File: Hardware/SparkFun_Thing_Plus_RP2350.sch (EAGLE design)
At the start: 84 parts, among them J1 THING_PLUS_LOGICAL, J3 QWIIC_RIGHT_ANGLE, J6 MICRO-SD-ATOM, Q1 100mA/20V/3.8Ω, U1 RP2350A, U2 RM2, U3 RT9080-33GJ5, U4 LM66200, U5 W25QXX128MBIT, U6 MCP73831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

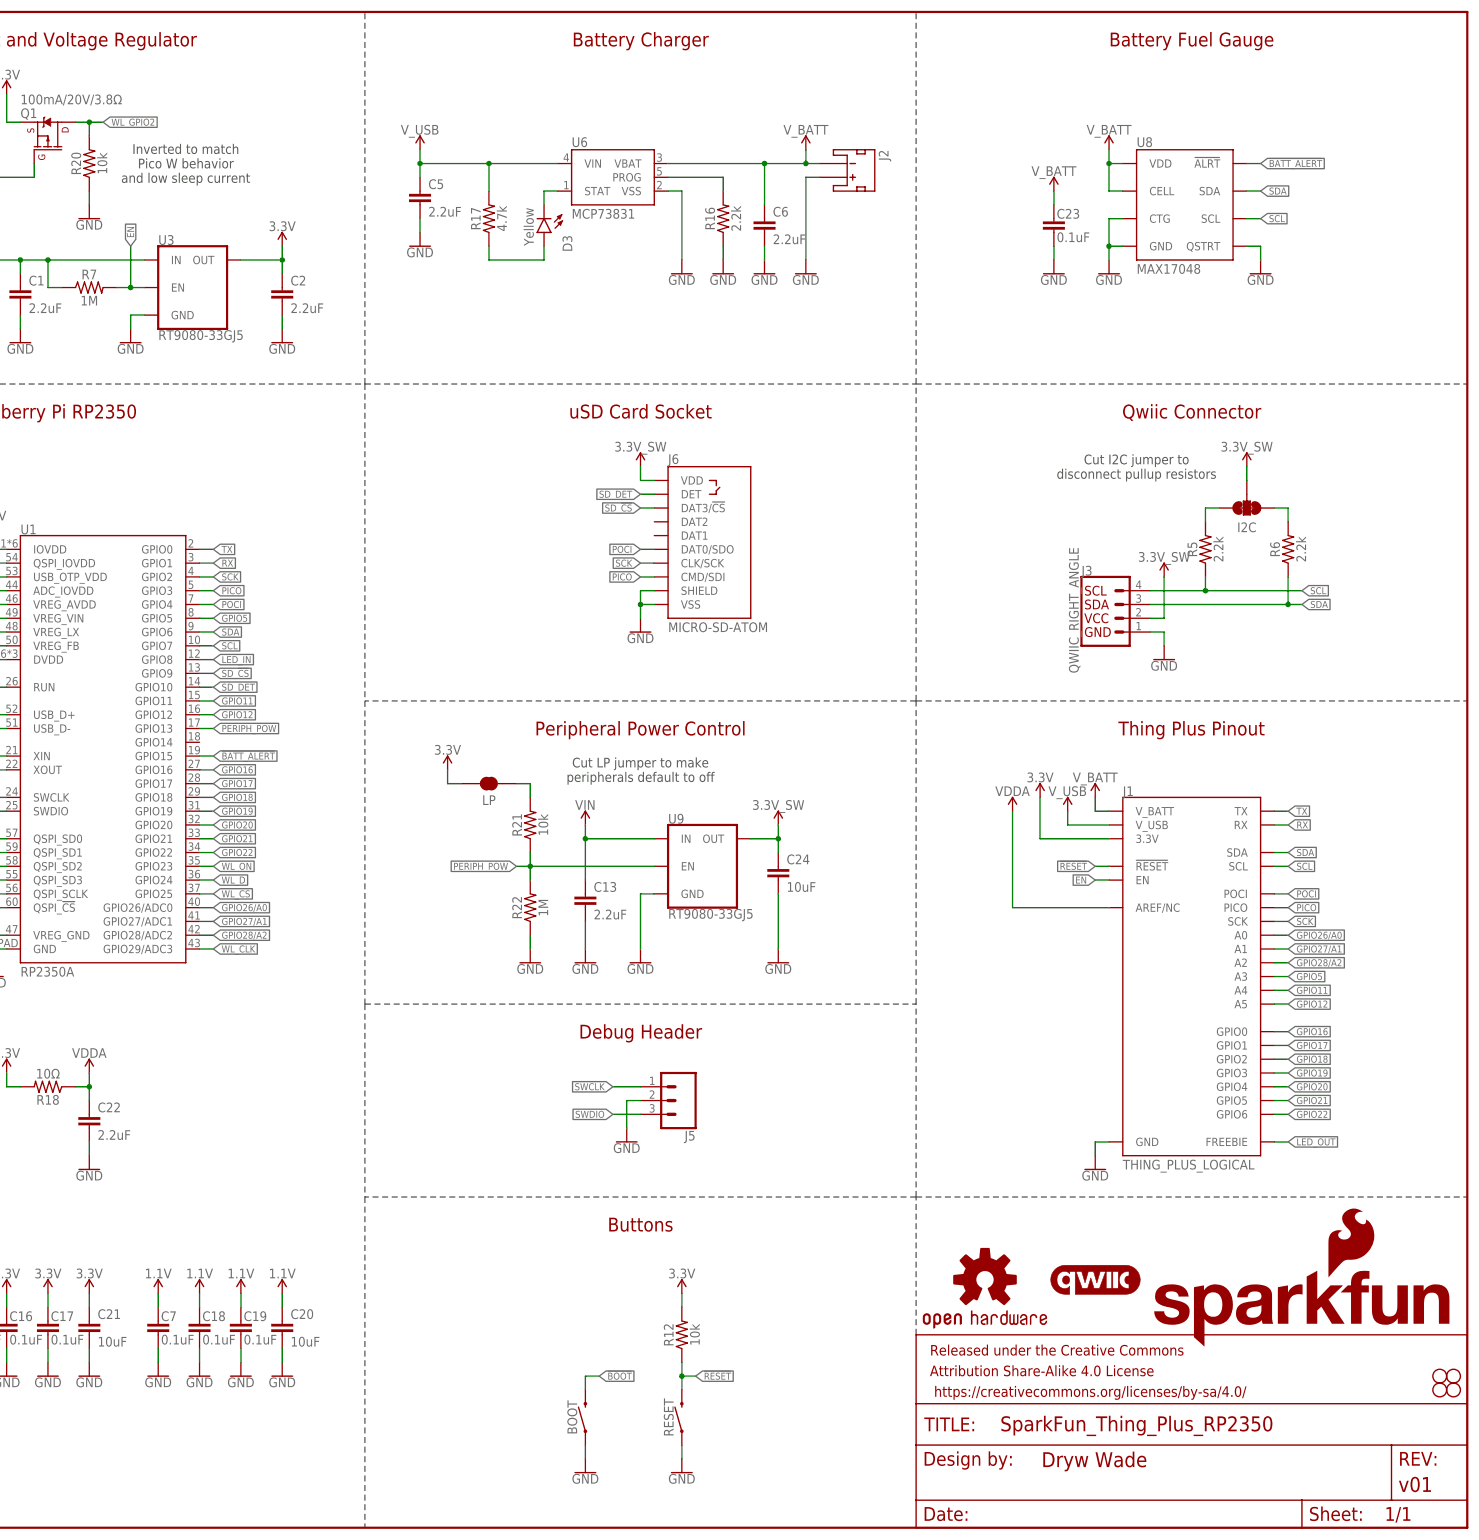
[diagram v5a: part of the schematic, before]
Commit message: Design review updates
Change version number to v02 (significant changes made since v01)
Add version number to copper
Add voltage regulator voltage and current specifications to schematic
Fix swapped POCI and PICO silk
Add test point for BOOT button
Fix acid traps
Add GND vias for each decoupling cap of U1
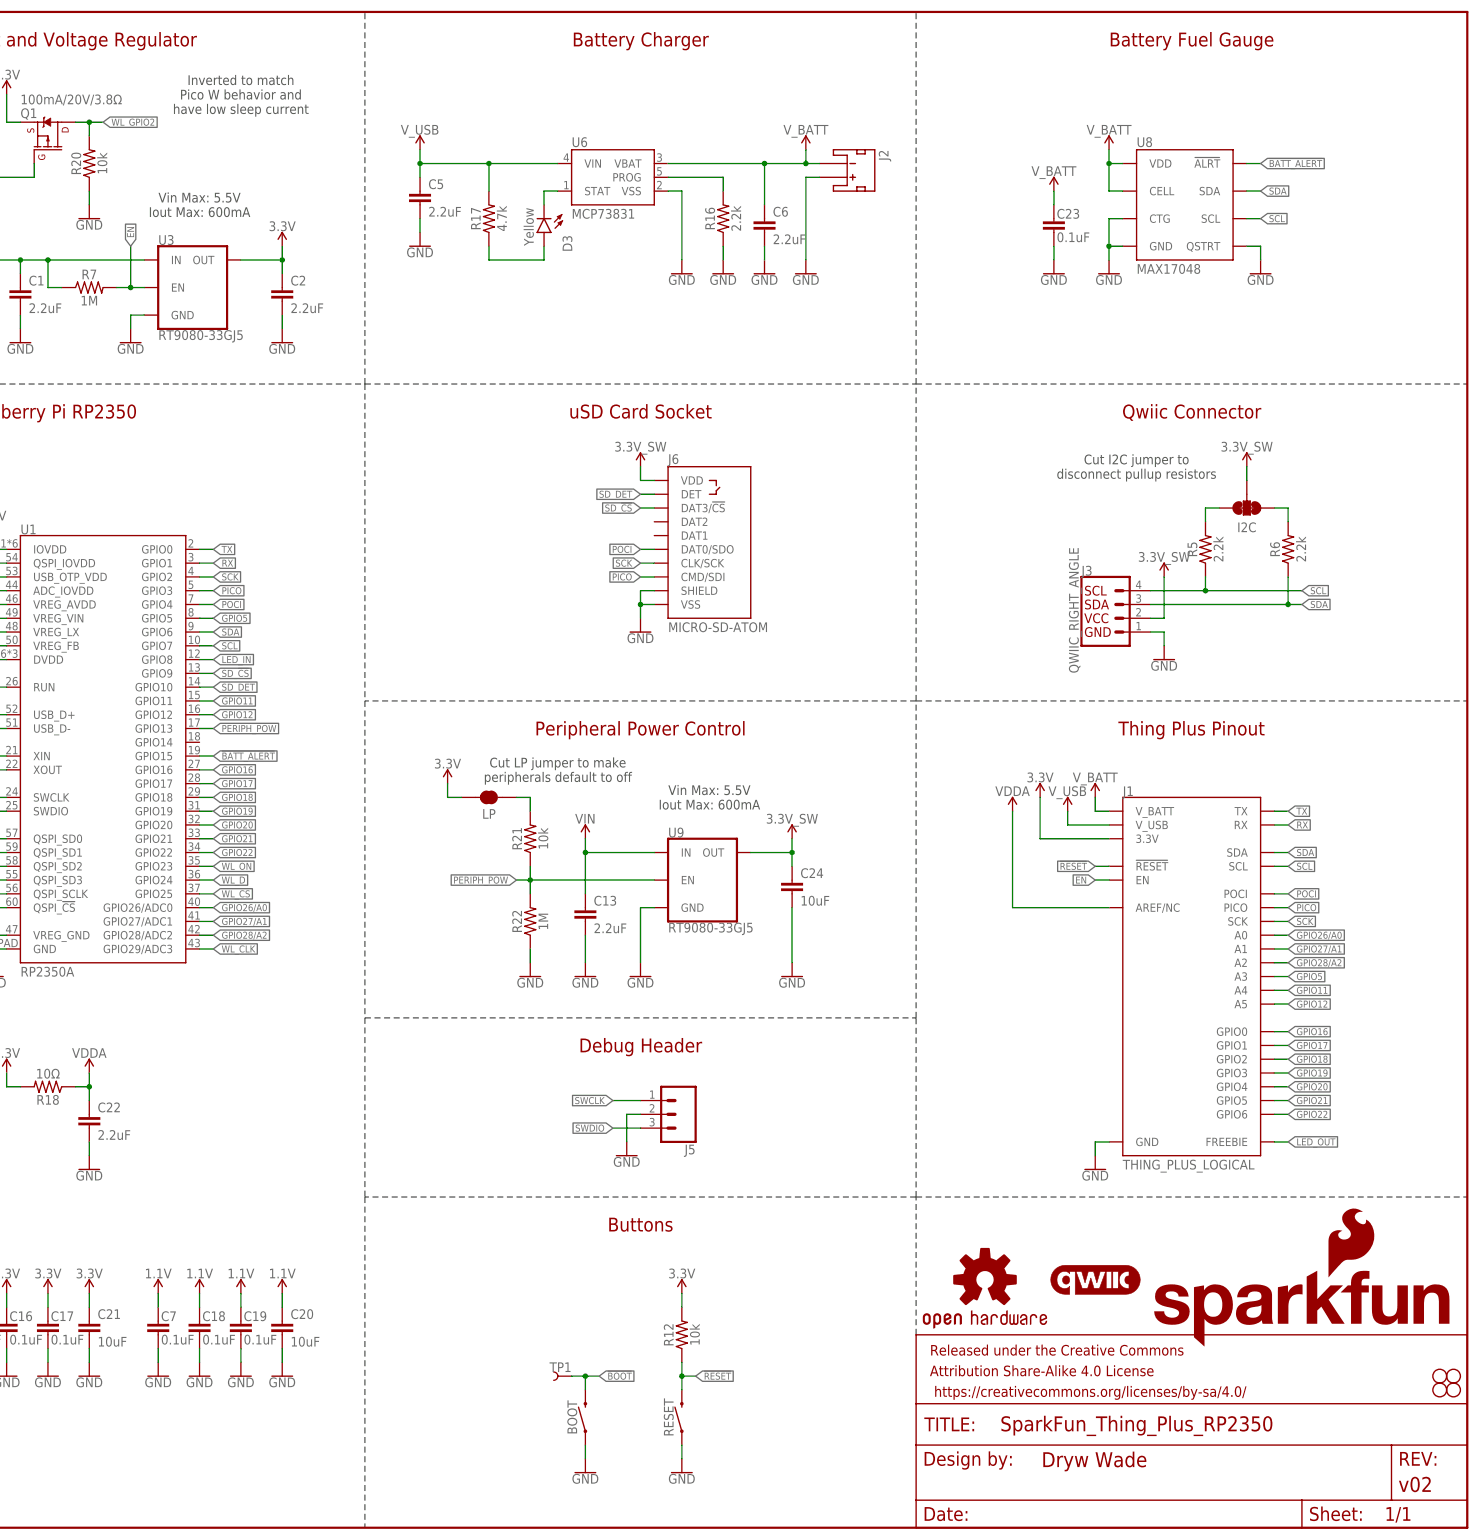
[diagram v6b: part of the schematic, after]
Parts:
- added TP1: TEST-POINT3X5, SparkFun-Connectors:TEST-POINT3X5
- FRAME1: REV v01 -> v02
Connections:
- net !BOOT!: now also TP1.1
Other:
- note added: "Inverted to match Pico W behavior and have low sleep current"
- note added: "Vin Max: 5.5V Iout Max: 600mA"
- note removed: "Inverted to match Pico W behavior and low sleep current"
- moved on the sheet: C13, C24, J5, LP, R21, R22, U9

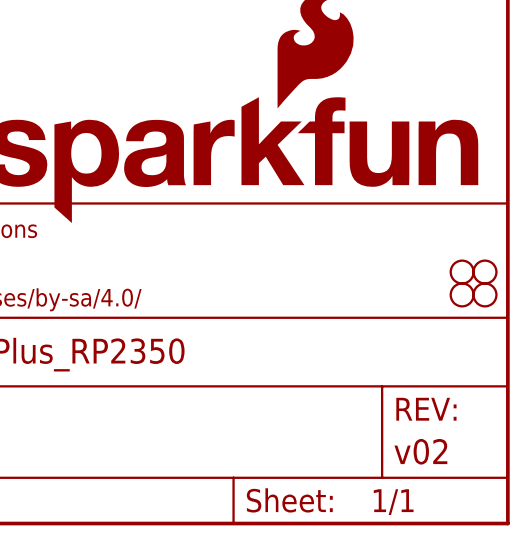
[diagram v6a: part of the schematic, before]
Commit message: Design review updates
Reposition fuel gauge and charge LED to get more clearance around them
Reposition power LED and resistor for better clearance
Add fiducials
Add measures
Fix TX and RX Buzzard tails
Fix acid trap
Improve GND pours
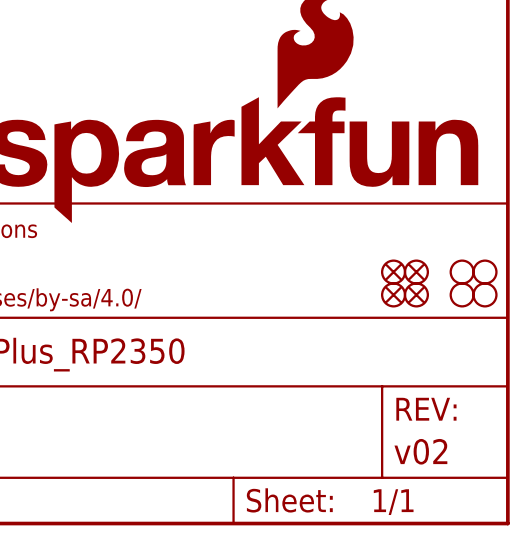
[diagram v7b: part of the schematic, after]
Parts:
- added FD1, FD2, FD3, FD4: FIDUCIALUFIDUCIAL, SparkFun-Aesthetics:FIDUCIALUFIDUCIAL
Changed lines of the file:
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@@
 <part name="SUPPLY47" library="SparkFun-PowerSymbols" deviceset="3.3V_SW" device=""/>
 <part name="TP1" library="SparkFun-Connectors" deviceset="TEST-POINT" device="3X5" value="TEST-POINT3X5"/>
+<part name="FD1" library="SparkFun-Aesthetics" deviceset="FIDUCIAL" device="UFIDUCIAL" value="FIDUCIALUFIDUCIAL"/>
+<part name="FD2" library="SparkFun-Aesthetics" deviceset="FIDUCIAL" device="UFIDUCIAL" value="FIDUCIALUFIDUCIAL"/>
+<part name="FD3" library="SparkFun-Aesthetics" deviceset="FIDUCIAL" device="UFIDUCIAL" value="FIDUCIALUFIDUCIAL"/>
+<part name="FD4" library="SparkFun-Aesthetics" deviceset="FIDUCIAL" device="UFIDUCIAL" value="FIDUCIALUFIDUCIAL"/>
 </parts>
 <sheets>
@@
 <attribute name="NAME" x="266.7" y="30.48" size="1.778" layer="95" font="vector" rot="R180"/>
 </instance>
+<instance part="FD1" gate="G$1" x="421.64" y="25.4" smashed="yes" rot="R90"/>
+<instance part="FD2" gate="G$1" x="421.64" y="27.94" smashed="yes" rot="R90"/>
+<instance part="FD3" gate="G$1" x="419.1" y="27.94" smashed="yes" rot="R90"/>
+<instance part="FD4" gate="G$1" x="419.1" y="25.4" smashed="yes" rot="R90"/>
 </instances>
 <busses>

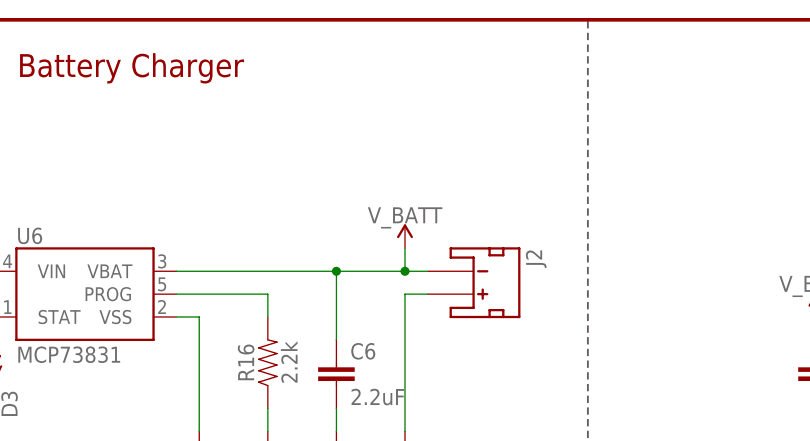
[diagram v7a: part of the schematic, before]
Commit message: Improve GND stitching
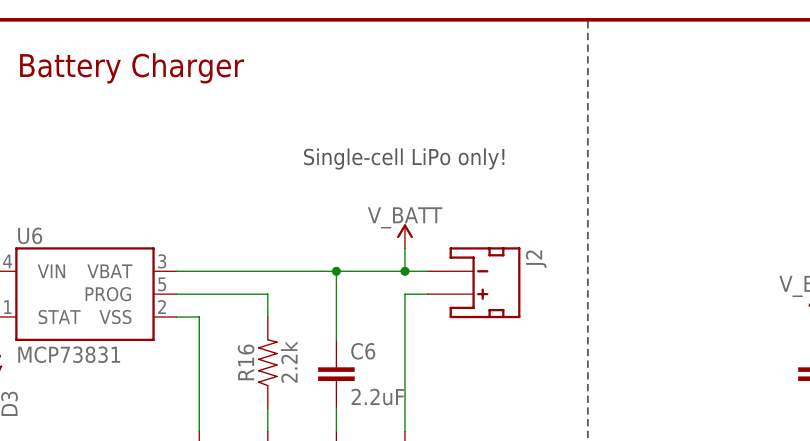
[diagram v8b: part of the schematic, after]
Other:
- note added: "Single-cell LiPo only!"
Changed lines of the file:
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@@
 Iout Max: 600mA</text>
 <text x="180.34" y="187.96" size="1.778" layer="97" font="vector" align="center"></text>
+<text x="309.88" y="264.16" size="1.778" layer="97" font="vector" align="center">Single-cell LiPo only!</text>
 </plain>
 <instances>
